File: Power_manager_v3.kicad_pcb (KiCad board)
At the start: 4 copper layers, 50 x 25 mm, 94 parts, among them J1 L_input, J2 Pow_mng_pow, J3 Load1, J4 Load2, J5 SWD (PLS5), J6 Dig_mod_iface, Q1 2N5551S, Q2 2N5551S, Q3 BSS138, U1 DC12003, U2 G3MB-202PL, U3 G3MB-202PL, U4 STM32F030F4Px, U5 HLW8112, U6 ADuM1251ARZ, U7 ADuM1201AR, U8 LM1117-3.3, Y1 CSTCE8M, Y2 ABLS-3.579545MHZ-D-3-Y-T

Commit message: Окончена трассировка печатной платы
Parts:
- removed C19, C25, C27, C32: 10uF, Capacitor_SMD:C_0603_1608Metric
- removed C20, C24, C28, C30, C31: 100nF, Capacitor_SMD:C_0603_1608Metric
- removed C21, C22: 22pF, Capacitor_SMD:C_0603_1608Metric
- removed D7: +3.3V, LED_SMD:LED_0603_1608Metric
- removed PS1: B0505S, Modules:B0505S
- removed Q3: BSS138, Package_TO_SOT_SMD:SOT-23
- removed the R16 at (90.2, 93.7)
- removed the R21 at (85.5, 94.8)
- removed R28, R37: 10k, Resistor_SMD:R_0603_1608Metric
- removed U8: LM1117-3.3, Package_TO_SOT_SMD:SOT-223-3_TabPin2
- added C14: 100nF, Capacitor_SMD:C_0603_1608Metric, B.Cu at (96.3, 93.8)
- added C16: 100nF, Capacitor_SMD:C_0603_1608Metric, F.Cu at (91.5, 84.1)
- added GND1: TestPoint_Small, TestPoint:TestPoint_THTPad_D2.0mm_Drill1.0mm, B.Cu at (78.5, 86.7)
- added R14: 10k, Resistor_SMD:R_0603_1608Metric, B.Cu at (78.7, 90.2)
- added R17: 332k, Resistor_SMD:R_0805_2012Metric, B.Cu at (96.5, 96.7)
- C15, C8, L1: moved to B.Cu
- C17, C18: value 100nF -> 22pF; moved to B.Cu
- C3, J5, JP1, R1: moved to F.Cu
- C4: value 100nF -> 10pF
- C6: value 10pF -> 10uF; moved to B.Cu
- C7: value 10uF -> 100nF
- D5: value +5P -> +5V; moved to B.Cu
- D6: value LM66100DCKR -> +3.3VP; footprint Modules:SOP65P210X110-6N -> LED_SMD:LED_0603_1608Metric; moved to B.Cu
- J6: footprint Connector_PinSocket_1.27mm:PinSocket_2x05_P1.27mm_Horizontal -> Connector_PinSocket_1.27mm:PinSocket_2x03_P1.27mm_Horizontal
- JP2: value 5V_en -> N_en
- JP3: value BOOT0 -> 5V_en; footprint Jumper:SolderJumper-2_P1.3mm_Open_RoundedPad1.0x1.5mm -> Jumper:SolderJumper-2_P1.3mm_Open_TrianglePad1.0x1.5mm; moved to F.Cu
- JP4: value 5VL_en -> Jumper_2x2_Open; footprint Jumper:SolderJumper-2_P1.3mm_Open_TrianglePad1.0x1.5mm -> Modules:PinHeader_2x02_P1.27mm_Vertical; moved to B.Cu
- JP5: value N_en -> 5VP_en
- JP6: value 3V3_en -> 3.3VP_en
- KP1: footprint TestPoint:TestPoint_Pad_1.0x1.0mm -> TestPoint:TestPoint_THTPad_D1.5mm_Drill0.7mm; moved to F.Cu
- R11: value 10k -> 332k; footprint Resistor_SMD:R_0603_1608Metric -> Resistor_SMD:R_0805_2012Metric; moved to B.Cu
- R13: value 332k -> 10k; footprint Resistor_SMD:R_0805_2012Metric -> Resistor_SMD:R_0603_1608Metric; moved to B.Cu
- R22: value 10k -> 1k; footprint Resistor_SMD:R_0603_1608Metric -> Resistor_SMD:R_0805_2012Metric
- R23, R27: value 50 -> 10k
- R24: value 10k -> 50
- R26: value 2.2M -> 50; moved to B.Cu
- U4: value STM32F030F4Px -> DC5V_DC5V3V3_v3; footprint Package_SO:TSSOP-20_4.4x6.5mm_P0.65mm -> Modules:DC5V_DC5V3V3_v3; moved to B.Cu
- U5: value HLW8112 -> STM32F030F4Px; footprint Package_SO:SSOP-16_4.4x5.2mm_P0.65mm -> Package_SO:TSSOP-20_4.4x6.5mm_P0.65mm; moved to F.Cu
- U6: value ADuM1251ARZ -> HLW8112; footprint Package_SO:SOIC-8_3.9x4.9mm_P1.27mm -> Package_SO:SSOP-16_4.4x5.2mm_P0.65mm; moved to B.Cu
- U7: value ADuM1201AR -> ADuM_I2C_v3; footprint Package_SO:SOIC-8_3.9x4.9mm_P1.27mm -> Modules:ADuM_I2C_Horizontal; moved to F.Cu
- moved R25 26.6 mm to (104.1, 80.9), turned to 90 degrees
- moved JP3 25.3 mm to (84.3, 77.0), turned to 90 degrees
- moved C7 24.4 mm to (106.3, 81.1), turned to 0 degrees
- moved R11 23.1 mm to (92.9, 97.5), turned to 180 degrees
- moved C8 22.3 mm to (83.7, 77.8), turned to 90 degrees
- moved R26 18.9 mm to (98.8, 83.0), turned to 180 degrees
- moved C17 18.7 mm to (99.7, 76.9), turned to 270 degrees
- moved R13 17.9 mm to (78.6, 84.4), turned to 0 degrees
- moved C4 16.9 mm to (96.2, 76.9), turned to 90 degrees
- moved JP4 16.6 mm to (102.5, 76.6), turned to 270 degrees
- moved C18 16.3 mm to (97.7, 76.9), turned to 270 degrees
- moved C13 14.7 mm to (100.1, 94.5), turned to 180 degrees
- moved J6 13.8 mm to (92.0, 81.0)
- moved C6 13.6 mm to (85.3, 77.8)
- moved R24 12.7 mm to (94.9, 83.0), turned to 0 degrees
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- renumbered R14 to R15, R15 to R16, R17 to R18, R18 to R19, R19 to R20, R20 to R21
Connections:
- C15 pad 2: Net-(C15-Pad2) -> +3.3VP
- C17 pad 2: +3.3VP -> Net-(C17-Pad2)
- C23 pad 1: Net-(C23-Pad1) -> +3.3VP
- C23 pad 2: Net-(C23-Pad2) -> GNDPWR
- C3 pad 2: +5P -> +5V
- C4 pad 1: GND1 -> Net-(C4-Pad1)
- C4 pad 2: /+5P0 -> GNDPWR
- C6 pad 1: Net-(C6-Pad1) -> GND1
- C6 pad 2: GNDPWR -> Net-(C6-Pad2)
- C7 pad 1: GND1 -> /nRst
- C7 pad 2: /+5P0 -> GNDPWR
- C8 pad 1: /nRst -> GND1
- C8 pad 2: GNDPWR -> Net-(C6-Pad2)
- D1 pad 2: +5VL -> +5VP
- D2 pad 2: +5VL -> +5VP
- D3 pad 1: +5VL -> +5VP
- D4 pad 1: +5VL -> +5VP
- D6 pad 1: +5P -> GNDPWR
- D6 pad 2: GND1 -> Net-(D6-Pad2)
- J1 pad 2: Net-(J1-Pad2) -> (no net)
- J1 pad 3: GNDPWR -> Net-(J1-Pad3)
- J2 pad 1: +5VP -> +5V
- J2 pad 2: +5VP -> +5V
- J3 pad 2: Net-(J3-Pad2) -> (no net)
- J4 pad 2: Net-(J4-Pad2) -> (no net)
- J6 pad 3: /scl0 -> /+5V_state
- J6 pad 4: /scl0 -> /I2C_Int
- J6 pad 5: /sda0 -> /scl0
- JP2 pad 1: /+5P0 -> Net-(J1-Pad3)
- JP2 pad 2: +5VP -> GNDPWR
- JP3 pad 1: GNDPWR -> +5V
- JP3 pad 2: Net-(JP3-Pad2) -> Net-(C6-Pad2)
- JP4 pad 1: Net-(C23-Pad2) -> GNDPWR
- JP4 pad 2: +5VL -> Net-(JP4-Pad2)
- JP5 pad 1: Net-(C23-Pad1) -> Net-(JP5-Pad1)
- JP5 pad 2: GNDPWR -> +5VP
- JP6 pad 1: Net-(C31-Pad2) -> Net-(JP6-Pad1)
- L1 pad 2: Net-(C18-Pad2) -> Net-(C16-Pad2)
- R11 pad 1: Net-(D5-Pad2) -> Net-(R11-Pad1)
- R11 pad 2: +5P -> Net-(R11-Pad2)
- R12 pad 1: Net-(R12-Pad1) -> Net-(R11-Pad2)
- R12 pad 2: Net-(R12-Pad2) -> AC
- R13 pad 1: Net-(R12-Pad2) -> Net-(D5-Pad2)
- R13 pad 2: AC -> +5V
- R22 pad 1: Net-(JP3-Pad2) -> Net-(C13-Pad2)
- R22 pad 2: +3.3VP -> GNDPWR
- R23 pad 1: Net-(C6-Pad1) -> Net-(JP4-Pad2)
- R23 pad 2: Net-(R23-Pad2) -> +3.3VP
- R24 pad 1: +3.3VP -> Net-(C5-Pad1)
- R24 pad 2: /nRst -> Net-(R24-Pad2)
- R25 pad 1: /+5P0 -> +3.3VP
- R25 pad 2: Net-(D6-Pad5) -> /nRst
- R26 pad 1: /+5V_state -> Net-(R26-Pad1)
- R26 pad 2: /+5P0 -> Net-(C18-Pad2)
- R27 pad 1: Net-(R27-Pad1) -> +3.3VP
- R27 pad 2: Net-(C22-Pad2) -> Net-(R27-Pad2)
- U1 pad 2: GNDPWR -> Net-(J1-Pad3)
- U1 pad 3: +5P -> +5V
- U2 pad 3: +5VL -> +5VP
- U3 pad 3: +5VL -> +5VP
- U4 pad 1: Net-(JP3-Pad2) -> Net-(C6-Pad2)
- U4 pad 2: Net-(C5-Pad1) -> GND1
- U4 pad 3: Net-(R23-Pad2) -> +5P
- U4 pad 4: /nRst -> /+5V_state
- U4 pad 5: Net-(C18-Pad2) -> Net-(JP5-Pad1)
- U4 pad 6: /Int -> GNDPWR
- U4 pad 7: /+5V_valid -> Net-(JP6-Pad1)
- U5 pad 1: Net-(C9-Pad2) -> Net-(JP4-Pad2)
- U5 pad 10: /SPI_SCLK -> /SPI_SSEL
- U5 pad 11: /SPI_SSEL -> /SPI_SCLK
- U5 pad 12: Net-(R28-Pad2) -> /SPI_MISO
- U5 pad 13: Net-(C21-Pad2) -> /SPI_MOSI
- U5 pad 14: Net-(R27-Pad1) -> /+5V_valid
- U5 pad 15: /Int -> GNDPWR
- U5 pad 2: Net-(C10-Pad1) -> Net-(C4-Pad1)
- U5 pad 3: Net-(C11-Pad2) -> Net-(R24-Pad2)
- U5 pad 4: Net-(C12-Pad1) -> /nRst
- U5 pad 5: Net-(C13-Pad2) -> Net-(C16-Pad2)
- U5 pad 6: GNDPWR -> /Int
- U5 pad 7: Net-(C15-Pad2) -> /L1_o1_nEn
- U5 pad 8: /SPI_MISO -> /L1_o2_nEn
- U5 pad 9: /SPI_MOSI -> Net-(KP1-Pad1)
- U6 pad 1: +3.3VP -> Net-(C9-Pad2)
- U6 pad 2: /I2C_SDA -> Net-(C10-Pad1)
- U6 pad 3: /I2C_SCL -> Net-(C11-Pad2)
- U6 pad 4: GNDPWR -> Net-(C12-Pad1)
- U6 pad 5: GND1 -> Net-(C13-Pad2)
- U6 pad 6: /scl0 -> GNDPWR
- U6 pad 7: /sda0 -> Net-(C14-Pad2)
- U6 pad 8: +5VP -> /SPI_MISO
- Y1 pad 1: Net-(C5-Pad1) -> Net-(C4-Pad1)
- Y1 pad 3: Net-(C6-Pad1) -> Net-(C5-Pad1)
- Y2 pad 1: Net-(C22-Pad2) -> Net-(C18-Pad2)
- Y2 pad 2: Net-(C21-Pad2) -> Net-(C17-Pad2)
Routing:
- net GNDPWR: track 61.2 -> 147.9 mm, vias 7 -> 13
- net AC: track 83.2 -> 41.7 mm, vias 2 -> 1
- net +5VP: track 20.8 -> 58.6 mm, vias 2 -> 1
- net +3.3VP: track 15.3 -> 51.5 mm, vias 3 -> 5
- net +5VL: track 31.3 -> 0.00 mm, vias 1 -> 0
- net /L1_o2_nEn: track 0.00 -> 27.0 mm, vias 0 -> 2
- net Net-(C12-Pad1): track 2.04 -> 24.1 mm, vias 0 -> 1
- net Net-(C11-Pad2): track 1.79 -> 22.4 mm, vias 0 -> 1
- net Net-(C31-Pad2): track 18.3 -> 0.00 mm, vias 2 -> 0
- net /+5V_valid: track 0.00 -> 17.7 mm, vias 0 -> 1
- net Net-(C16-Pad2): track 0.00 -> 15.2 mm, vias 0 -> 2
- net Net-(R27-Pad2): track 0.00 -> 14.8 mm, vias 0 -> 2
- net /+5P0: track 14.6 -> 0.00 mm
- net Net-(J1-Pad3): track 0.00 -> 12.1 mm
- net Net-(JP4-Pad2): track 0.00 -> 11.2 mm
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- removed copper zone on In2.Cu, net GNDPWR
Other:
- net class AC230V removed
- net class Digital added: clearance 0.2, trace_width 0.3, via_dia 0.8, via_drill 0.4
- board text added: "+3.3V"
- board text removed: "+3V3"

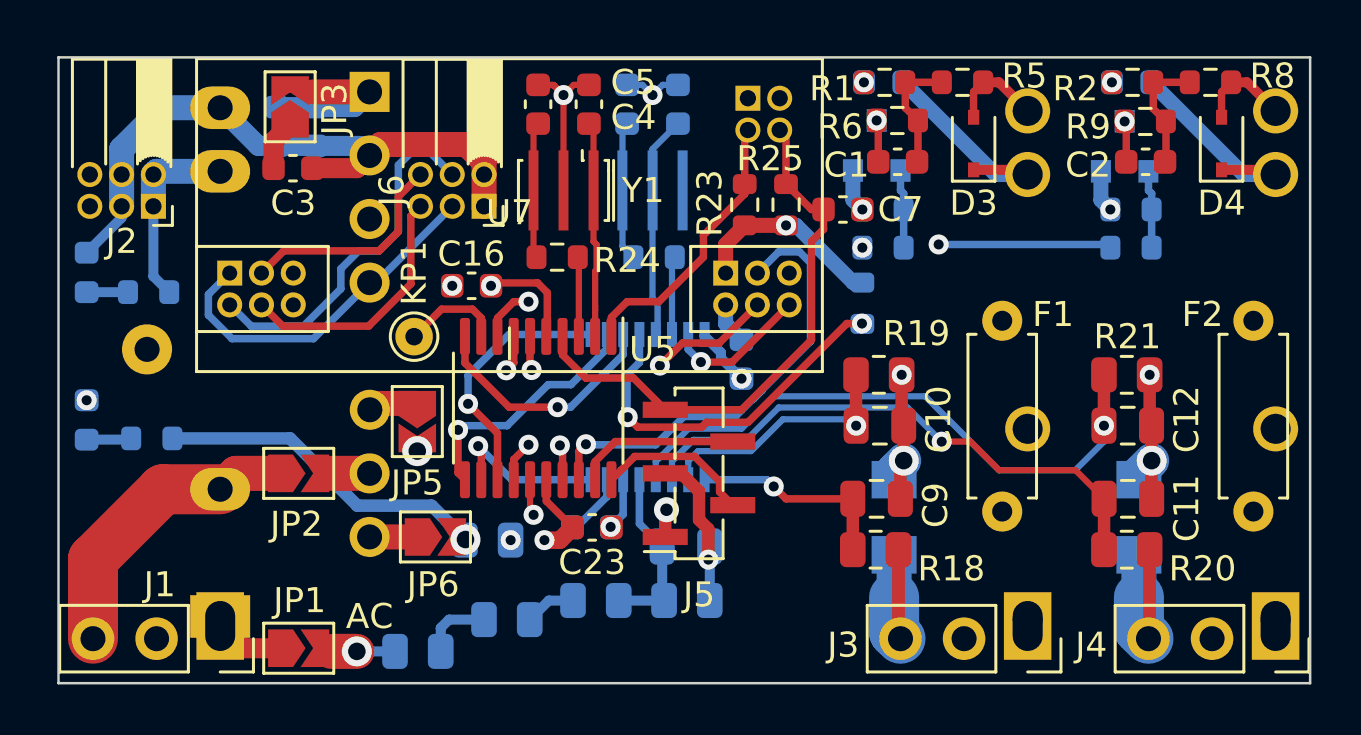
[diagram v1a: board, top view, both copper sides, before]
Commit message: Исправления в схеме и в печатной плате.
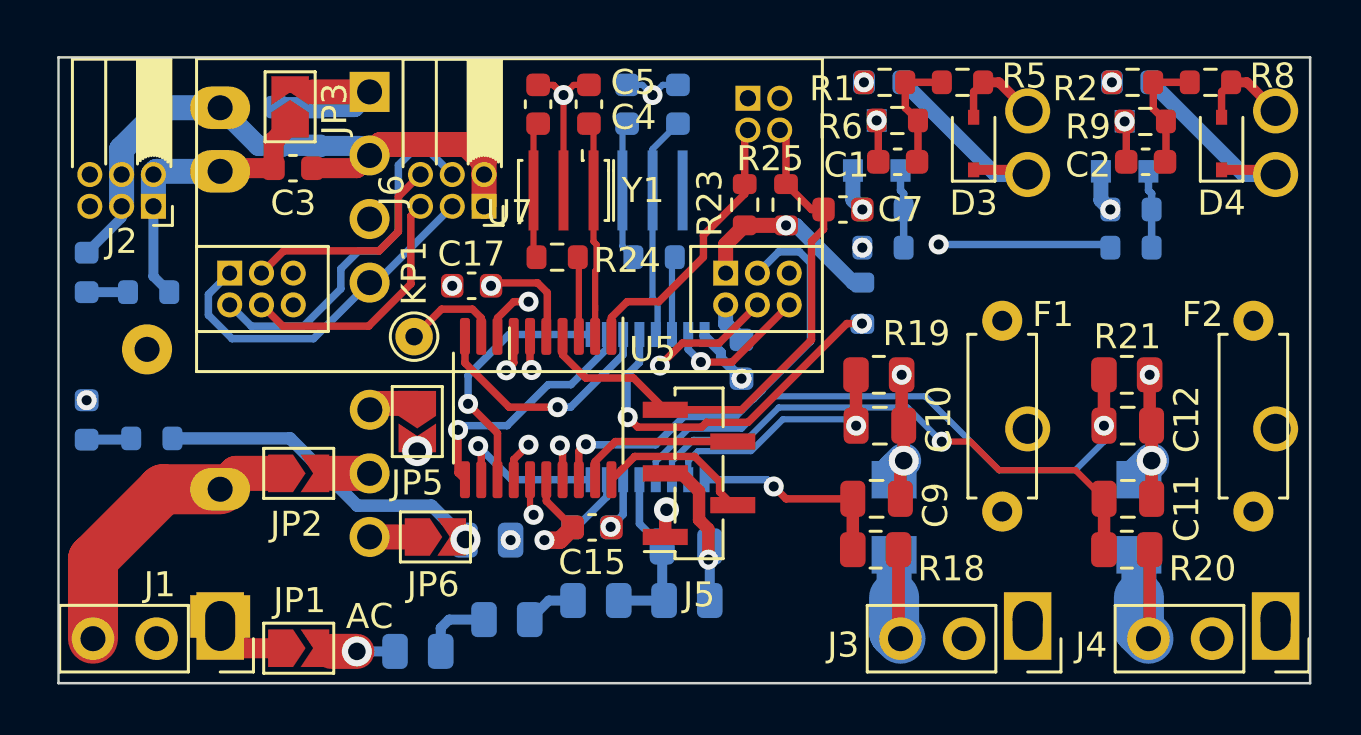
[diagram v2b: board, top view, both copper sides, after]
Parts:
- renumbered C23 to C15, C15 to C16, C16 to C17, C17 to C18, C18 to C19
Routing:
- net +5V: track 9.68 -> 11.9 mm

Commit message: Мелкие исправления в схеме и плате
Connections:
- J2 pad 1: +5V -> +5P
- J2 pad 2: +5V -> +5P
- J2 pad 5: +5P -> +5V
- J2 pad 6: +5P -> +5V
- J6 pad 1: GND1 -> /+5V_state
- J6 pad 2: GND1 -> /I2C_Int
- J6 pad 3: /+5V_state -> GND1
- J6 pad 4: /I2C_Int -> GND1
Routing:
- net +5V: track 11.9 -> 16.7 mm, vias 0 -> 1
- net +5P: track 16.0 -> 12.2 mm
- net GND1: track 39.4 -> 37.9 mm
- net /+5V_state: track 14.4 -> 15.9 mm
- net /I2C_Int: track 14.5 -> 16.0 mm
